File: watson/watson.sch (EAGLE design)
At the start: 37 parts, among them X1 2540-

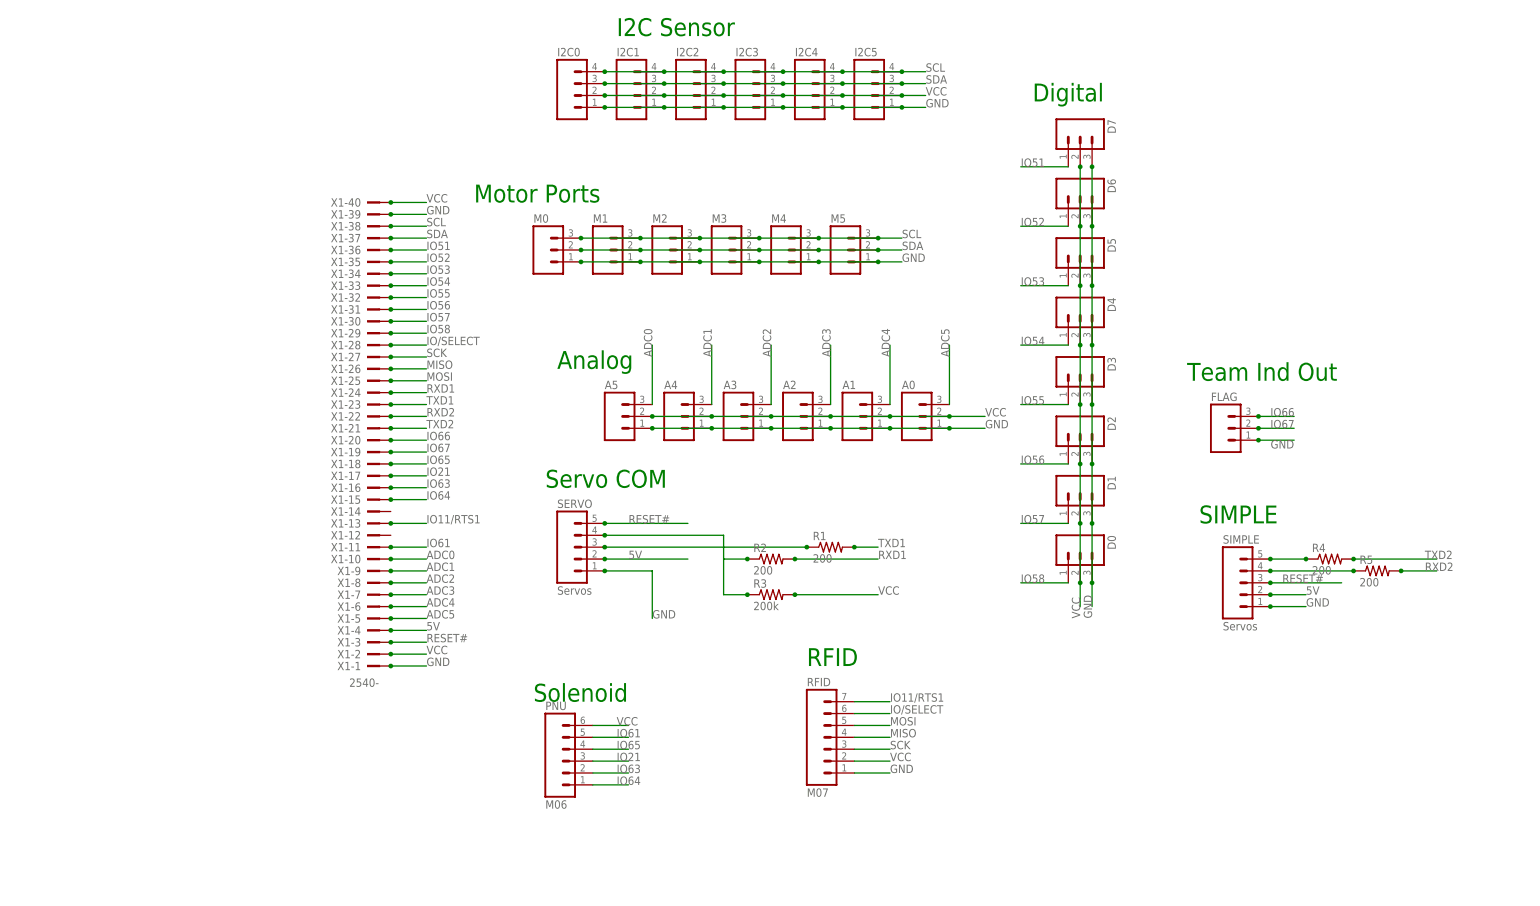
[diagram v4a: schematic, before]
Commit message: Sherlock, Watson, and Solenoid Rev E
- Updated all parts on all boards with their new
  versions in pie.lbr
- Cleaned up silkscreens and made names more
  meaningful
- Cleaned up schematics

This is intended to be the final version for all
three boards. There will be one more revision,
but that is only to add the copyright info Ryan
is making for the schematics and boards.

A side-effect of cleaning up the schematics is
that some connections may have been severd and
traces may have disappeared. I've tried my best
to detect and re-route those traces. If you find
any, please let me know. Thanks.

Sherlock DFM: https://www.freedfm.com/freedfm/0019486703422743/results/summary2.htm
Watson DFM: https://www.freedfm.com/freedfm/0019486703422746/results/summary2.htm
Solenoid DFM: https://www.freedfm.com/freedfm/0019486703422817/results/summary2.htm

Change-Id: I0ddac82c4f4e303a663db72d1e0729480dfd451e
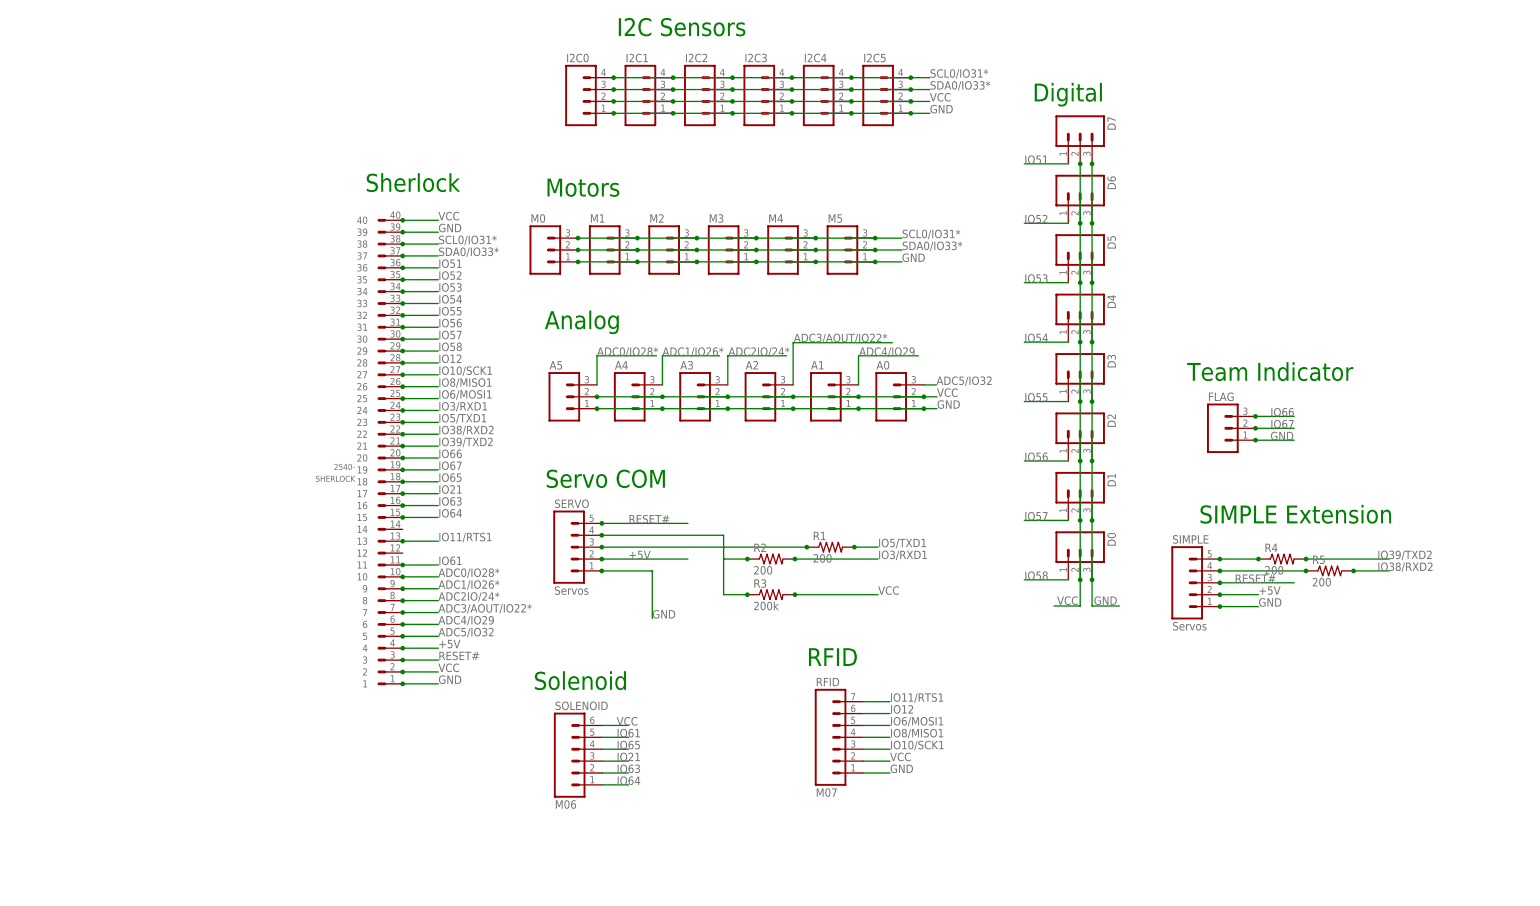
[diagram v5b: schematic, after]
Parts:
- removed PNU: M06, pie:M06
- removed X1: 2540-, pie:2540-
- added SHERLOCK: 2540-, pie:2540-
- added SOLENOID: M06, pie:M06
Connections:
- removed net 5V: SERVO.2, SIMPLE.2, X1-4.KL
- removed net ADC0: A5.3, X1-10.KL
- removed net ADC1: A4.3, X1-9.KL
- removed net ADC2: A3.3, X1-8.KL
- removed net ADC3: A2.3, X1-7.KL
- removed net ADC4: A1.3, X1-6.KL
- removed net ADC5: A0.3, X1-5.KL
- removed net IO/SELECT: RFID.6, X1-28.KL
- removed net MISO: RFID.4, X1-26.KL
- removed net MOSI: RFID.5, X1-25.KL
- removed net RXD1: R2.2, X1-24.KL
- removed net RXD2: R5.2, X1-22.KL
- removed net SCK: RFID.3, X1-27.KL
- removed net SCL: I2C0.4, I2C1.4, I2C2.4, I2C3.4, I2C4.4, I2C5.4, M0.3, M1.3, M2.3, M3.3, M4.3, M5.3, X1-38.KL
- removed net SDA: I2C0.3, I2C1.3, I2C2.3, I2C3.3, I2C4.3, I2C5.3, M0.2, M1.2, M2.2, M3.2, M4.2, M5.2, X1-37.KL
- removed net TXD1: R1.2, X1-23.KL
- removed net TXD2: R4.2, X1-21.KL
- new net +5V: SERVO.2, SHERLOCK.4, SIMPLE.2
- new net ADC0/IO28*: A5.3, SHERLOCK.10
- new net ADC1/IO26*: A4.3, SHERLOCK.9
- new net ADC2IO/24*: A3.3, SHERLOCK.8
- new net ADC3/AOUT/IO22*: A2.3, SHERLOCK.7
- new net ADC4/IO29: A1.3, SHERLOCK.6
- new net ADC5/IO32: A0.3, SHERLOCK.5
- new net IO10/SCK1: RFID.3, SHERLOCK.27
- new net IO12: RFID.6, SHERLOCK.28
- new net IO3/RXD1: R2.2, SHERLOCK.24
- new net IO38/RXD2: R5.2, SHERLOCK.22
- new net IO39/TXD2: R4.2, SHERLOCK.21
- new net IO5/TXD1: R1.2, SHERLOCK.23
- new net IO6/MOSI1: RFID.5, SHERLOCK.25
- new net IO8/MISO1: RFID.4, SHERLOCK.26
- new net SCL0/IO31*: I2C0.4, I2C1.4, I2C2.4, I2C3.4, I2C4.4, I2C5.4, M0.3, M1.3, M2.3, M3.3, M4.3, M5.3, SHERLOCK.38
- new net SDA0/IO33*: I2C0.3, I2C1.3, I2C2.3, I2C3.3, I2C4.3, I2C5.3, M0.2, M1.2, M2.2, M3.2, M4.2, M5.2, SHERLOCK.37
- net GND: now also SHERLOCK.1, SHERLOCK.39; no longer X1-1.KL, X1-39.KL
- net IO11/RTS1: now also SHERLOCK.13; no longer X1-13.KL
- net IO21: now also SHERLOCK.17, SOLENOID.3; no longer PNU.3, X1-17.KL
- net IO51: now also SHERLOCK.36; no longer X1-36.KL
- net IO52: now also SHERLOCK.35; no longer X1-35.KL
- net IO53: now also SHERLOCK.34; no longer X1-34.KL
- net IO54: now also SHERLOCK.33; no longer X1-33.KL
- net IO55: now also SHERLOCK.32; no longer X1-32.KL
- net IO56: now also SHERLOCK.31; no longer X1-31.KL
- net IO57: now also SHERLOCK.30; no longer X1-30.KL
- net IO58: now also SHERLOCK.29; no longer X1-29.KL
- net IO61: now also SHERLOCK.11, SOLENOID.5; no longer PNU.5, X1-11.KL
- net IO63: now also SHERLOCK.16, SOLENOID.2; no longer PNU.2, X1-16.KL
- net IO64: now also SHERLOCK.15, SOLENOID.1; no longer PNU.1, X1-15.KL
- net IO65: now also SHERLOCK.18, SOLENOID.4; no longer PNU.4, X1-18.KL
- net IO66: now also SHERLOCK.20; no longer X1-20.KL
- net IO67: now also SHERLOCK.19; no longer X1-19.KL
- net RESET#: now also SHERLOCK.3; no longer X1-3.KL
- net VCC: now also SHERLOCK.2, SHERLOCK.40, SOLENOID.6; no longer PNU.6, X1-2.KL, X1-40.KL
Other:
- note added: "I2C Sensors"
- note added: "Motors"
- note added: "SIMPLE Extension"
- note added: "Sherlock"
- note added: "Team Indicator"
- note removed: "I2C Sensor"
- note removed: "Motor Ports"
- note removed: "SIMPLE"
- note removed: "Team Ind Out"
- moved on the sheet: A0, A1, A2, A3, A4, A5, D0, D1, D2, D3, D4, D5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
